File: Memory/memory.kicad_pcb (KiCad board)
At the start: 2 copper layers, 95.3 x 81.3 mm, 55 parts, among them J1 Power, J2 Misc, J3 Address, J4 Bus, SW1 SW_Push, SW2 SW_DIP_x08, U1 74LS157, U2 74LS189, U3 74LS04, U4 74LS00, U5 74LS04, U6 74LS189, U7 74LS245, U8 74LS157, U9 74LS157

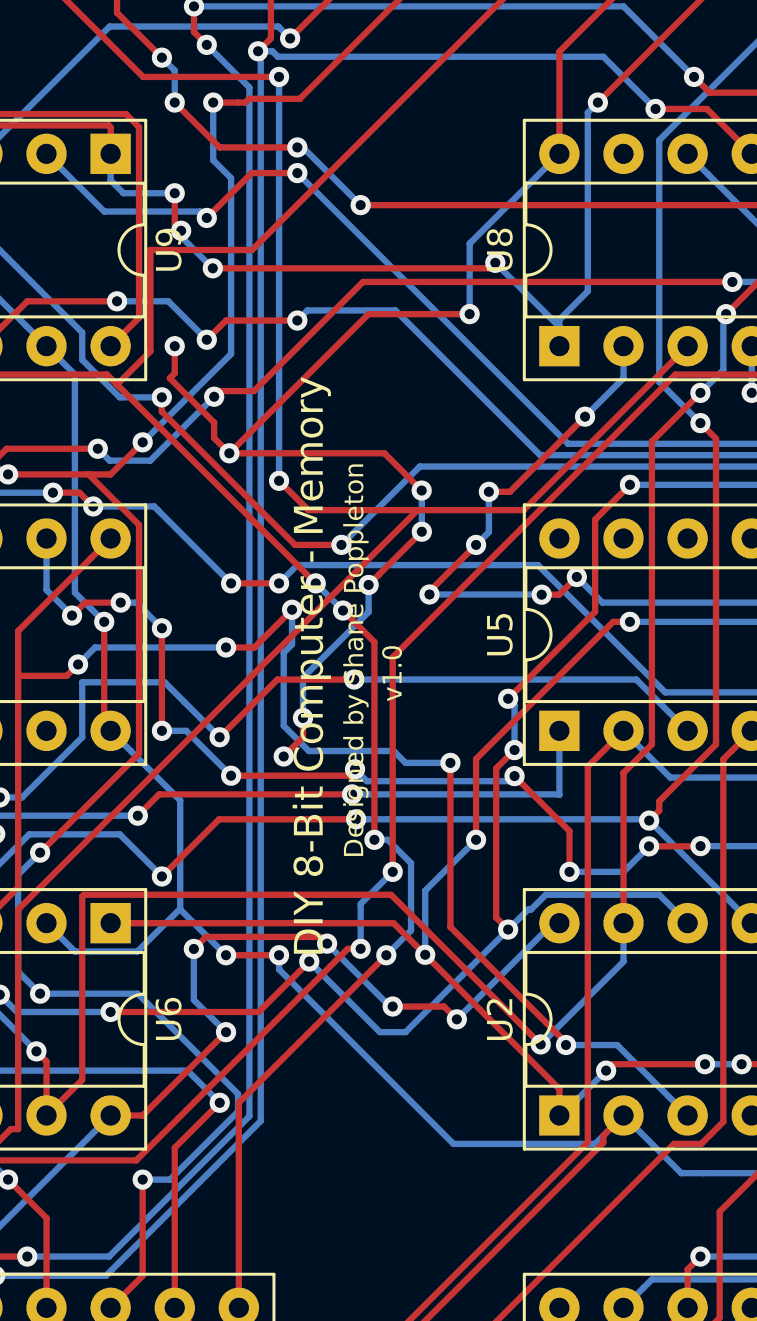
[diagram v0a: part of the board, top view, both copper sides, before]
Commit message: Added Attribution on each PCB, and regenerated gerbers
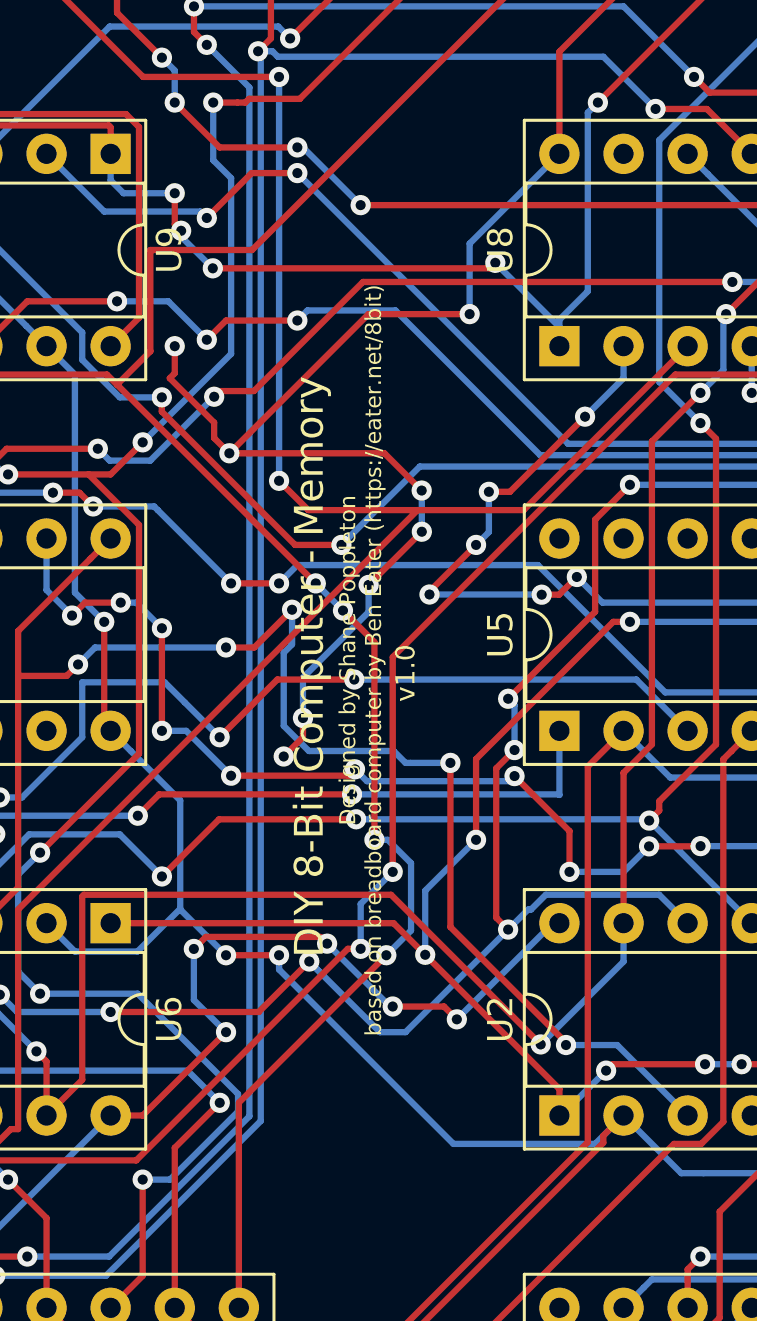
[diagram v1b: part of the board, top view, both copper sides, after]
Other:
- board text added: "Designed by Shane Poppleton based on breadboard computer by Ben Eater (https://eater.net/8bit)"
- board text removed: "Designed by Shane Poppleton"
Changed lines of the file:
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@@
     )
   )
-  (gr_text v1.0 (at 137.16 81.788 90) (layer F.SilkS)
+  (gr_text v1.0 (at 137.668 81.788 90) (layer F.SilkS)
     (effects (font (size 0.762 0.762) (thickness 0.127)))
   )
-  (gr_text "Designed by Shane Poppleton" (at 135.636 81.28 90) (layer F.SilkS)
-    (effects (font (size 0.762 0.762) (thickness 0.127)))
+  (gr_text "Designed by Shane Poppleton\nbased on breadboard computer by Ben Eater (https://eater.net/8bit)\n" (at 135.89 81.28 90) (layer F.SilkS)
+    (effects (font (size 0.635 0.635) (thickness 0.1016)))
   )
   (gr_text "DIY 8-Bit Computer - Memory" (at 133.858 81.534 90) (layer F.SilkS)
